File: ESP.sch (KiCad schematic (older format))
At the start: 2 parts, among them U301 LSF0204x, U302 ESP8266

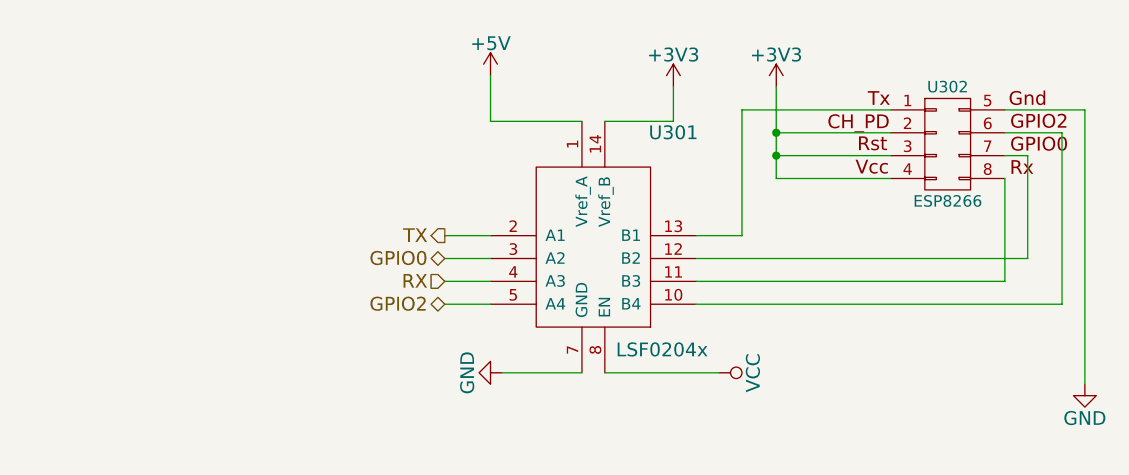
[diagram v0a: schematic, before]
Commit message: Redesign the board and add USB
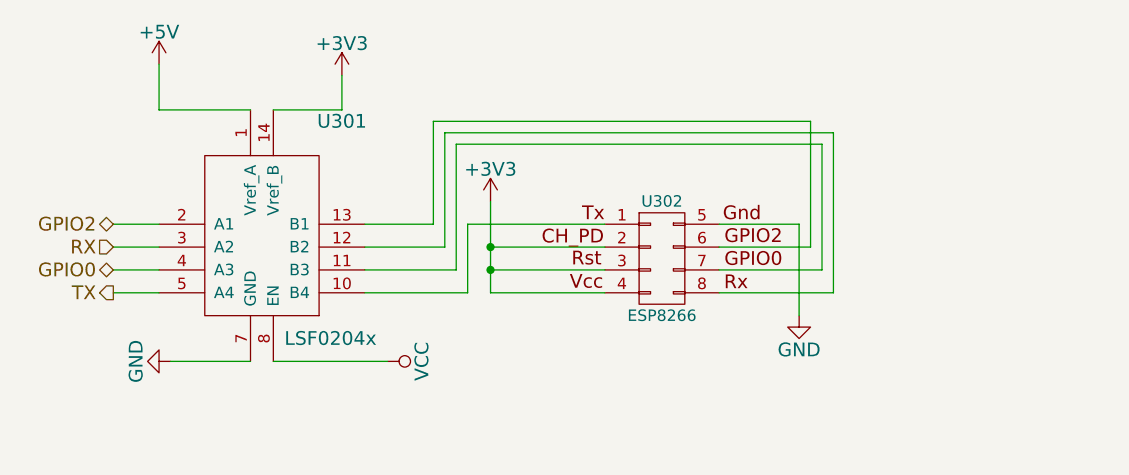
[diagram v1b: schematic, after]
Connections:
- net GPIO0: now also U301.4 (A3); no longer U301.3 (A2)
- net GPIO2: now also U301.2 (A1); no longer U301.5 (A4)
- net RX: now also U301.3 (A2); no longer U301.4 (A3)
- net TX: now also U301.5 (A4); no longer U301.2 (A1)
- net at U301.10 (B4): now also U302.1 (TX); no longer U302.6 (P4)
- net at U301.11 (B3): now also U302.7 (P6); no longer U302.8 (P8)
- net at U301.12 (B2): now also U302.8 (P8); no longer U302.7 (P6)
- net at U301.13 (B1): now also U302.6 (P4); no longer U302.1 (TX)
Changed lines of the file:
@@
 $Comp
 L LSF0204x U301
-U 1 1 55337A29
-P 4550 2300
-F 0 "U301" H 4900 2800 60  0000 C CNN
-F 1 "LSF0204x" H 4850 1850 60  0000 C CNN
-F 2 "" H 4550 2300 60  0000 C CNN
-F 3 "" H 4550 2300 60  0000 C CNN
-	1    4550 2300
+U 1 1 5538DE80
+P 3100 2250
+F 0 "U301" H 3450 2750 60  0000 C CNN
+F 1 "LSF0204x" H 3400 1800 60  0000 C CNN
+F 2 "" H 3100 2250 60  0000 C CNN
+F 3 "" H 3100 2250 60  0000 C CNN
+	1    3100 2250
 	1    0    0    -1
 $EndComp
 $Comp
 L ESP8266 U302
-U 1 1 55337A30
-P 6100 1850
-F 0 "U302" H 6100 2100 50  0000 C CNN
-F 1 "ESP8266" H 6100 1600 50  0000 C CNN
-F 2 "" H 6100 650 60  0000 C CNN
-F 3 "" H 6100 650 60  0000 C CNN
-	1    6100 1850
+U 1 1 5538DE86
+P 4850 2350
+F 0 "U302" H 4850 2600 50  0000 C CNN
+F 1 "ESP8266" H 4850 2100 50  0000 C CNN
+F 2 "" H 4850 1150 60  0000 C CNN
+F 3 "" H 4850 1150 60  0000 C CNN
+	1    4850 2350
+	1    0    0    -1
+$EndComp
+$Comp
+L VCC #PWR012
+U 1 1 5538DE95
+P 3650 2800
+F 0 "#PWR012" H 3650 2650 60  0001 C CNN
+F 1 "VCC" H 3650 2950 60  0000 C CNN
+F 2 "" H 3650 2800 60  0000 C CNN
+F 3 "" H 3650 2800 60  0000 C CNN
+	1    3650 2800
+	0    1    1    0
+$EndComp
+$Comp
+L +5V #PWR013
+U 1 1 5538DE9F
+P 2650 1500
+F 0 "#PWR013" H 2650 1350 60  0001 C CNN
+F 1 "+5V" H 2650 1640 60  0000 C CNN
+F 2 "" H 2650 1500 60  0000 C CNN
+F 3 "" H 2650 1500 60  0000 C CNN
+	1    2650 1500
+	1    0    0    -1
+$EndComp
+$Comp
+L +3V3 #PWR014
+U 1 1 5538DEAA
+P 3450 1550
+F 0 "#PWR014" H 3450 1400 60  0001 C CNN
+F 1 "+3V3" H 3450 1690 60  0000 C CNN
+F 2 "" H 3450 1550 60  0000 C CNN
+F 3 "" H 3450 1550 60  0000 C CNN
+	1    3450 1550
+	1    0    0    -1
+$EndComp
+$Comp
+L GND #PWR015
+U 1 1 5538DEB0
+P 2700 2800
+F 0 "#PWR015" H 2700 2550 60  0001 C CNN
+F 1 "GND" H 2700 2650 60  0000 C CNN
+F 2 "" H 2700 2800 60  0000 C CNN
+F 3 "" H 2700 2800 60  0000 C CNN
+	1    2700 2800
+	0    1    1    0
+$EndComp
+$Comp
+L GND #PWR016
+U 1 1 5538DEB7
+P 5450 2600
+F 0 "#PWR016" H 5450 2350 60  0001 C CNN
+F 1 "GND" H 5450 2450 60  0000 C CNN
+F 2 "" H 5450 2600 60  0000 C CNN
+F 3 "" H 5450 2600 60  0000 C CNN
+	1    5450 2600
+	1    0    0    -1
+$EndComp
+Text HLabel 2450 2500 0    60   Output ~ 0
+TX
+Text HLabel 2450 2400 0    60   BiDi ~ 0
+GPIO0
+Text HLabel 2450 2300 0    60   Input ~ 0
+RX
+Text HLabel 2450 2200 0    60   BiDi ~ 0
+GPIO2
+$Comp
+L +3V3 #PWR017
+U 1 1 5538DEC8
+P 4100 2100
+F 0 "#PWR017" H 4100 1950 60  0001 C CNN
+F 1 "+3V3" H 4100 2240 60  0000 C CNN
+F 2 "" H 4100 2100 60  0000 C CNN
+F 3 "" H 4100 2100 60  0000 C CNN
+	1    4100 2100
 	1    0    0    -1
 $EndComp
 Wire Wire Line
-	6350 2000 6350 2450
+	3150 2800 3650 2800
 Wire Wire Line
-	5000 2350 6450 2350
+	2650 1700 3050 1700
 Wire Wire Line
-	6450 2350 6450 1900
+	2650 1500 2650 1700
 Wire Wire Line
-	6450 1900 6350 1900
+	3150 1700 3450 1700
 Wire Wire Line
-	5850 1700 5200 1700
+	3450 1700 3450 1550
 Wire Wire Line
-	5000 2550 6600 2550
+	4100 2500 4600 2500
 Wire Wire Line
-	6600 2550 6600 1800
+	4100 2400 4600 2400
 Wire Wire Line
-	6600 1800 6350 1800
+	4100 2300 4600 2300
 Wire Wire Line
-	4600 2850 5100 2850
-$Comp
-L VCC #PWR010
-U 1 1 55337A40
-P 5100 2850
-F 0 "#PWR010" H 5100 2700 60  0001 C CNN
-F 1 "VCC" H 5100 3000 60  0000 C CNN
-F 2 "" H 5100 2850 60  0000 C CNN
-F 3 "" H 5100 2850 60  0000 C CNN
-	1    5100 2850
-	0    1    1    0
-$EndComp
+	2700 2800 3050 2800
 Wire Wire Line
-	4100 1750 4500 1750
+	4100 2100 4100 2500
+Connection ~ 4100 2400
+Connection ~ 4100 2300
 Wire Wire Line
-	4100 1550 4100 1750
+	2650 2200 2450 2200
 Wire Wire Line
-	4600 1750 4900 1750
+	2450 2300 2650 2300
 Wire Wire Line
-	4900 1750 4900 1600
-$Comp
-L +5V #PWR011
-U 1 1 55337A4A
-P 4100 1550
-F 0 "#PWR011" H 4100 1400 60  0001 C CNN
-F 1 "+5V" H 4100 1690 60  0000 C CNN
-F 2 "" H 4100 1550 60  0000 C CNN
-F 3 "" H 4100 1550 60  0000 C CNN
-	1    4100 1550
-	1    0    0    -1
-$EndComp
+	2450 2400 2650 2400
 Wire Wire Line
-	6350 1700 6700 1700
+	2450 2500 2650 2500
 Wire Wire Line
-	6700 1700 6700 2900
+	4600 2200 4000 2200
 Wire Wire Line
-	5350 2000 5850 2000
+	4000 2200 4000 2500
 Wire Wire Line
-	5350 1900 5850 1900
+	4000 2500 3550 2500
 Wire Wire Line
-	5350 1800 5850 1800
-$Comp
-L +3V3 #PWR012
-U 1 1 55337A58
-P 4900 1600
-F 0 "#PWR012" H 4900 1450 60  0001 C CNN
-F 1 "+3V3" H 4900 1740 60  0000 C CNN
-F 2 "" H 4900 1600 60  0000 C CNN
-F 3 "" H 4900 1600 60  0000 C CNN
-	1    4900 1600
-	1    0    0    -1
-$EndComp
-$Comp
-L GND #PWR013
-U 1 1 55337A5E
-P 4150 2850
-F 0 "#PWR013" H 4150 2600 60  0001 C CNN
-F 1 "GND" H 4150 2700 60  0000 C CNN
-F 2 "" H 4150 2850 60  0000 C CNN
-F 3 "" H 4150 2850 60  0000 C CNN
-	1    4150 2850
-	0    1    1    0
-$EndComp
+	3550 2400 3950 2400
 Wire Wire Line
-	4150 2850 4500 2850
-$Comp
-L GND #PWR014
-U 1 1 55337A65
-P 6700 2900
-F 0 "#PWR014" H 6700 2650 60  0001 C CNN
-F 1 "GND" H 6700 2750 60  0000 C CNN
-F 2 "" H 6700 2900 60  0000 C CNN
-F 3 "" H 6700 2900 60  0000 C CNN
-	1    6700 2900
-	1    0    0    -1
-$EndComp
+	3950 2400 3950 1850
 Wire Wire Line
-	4100 2250 3900 2250
+	3950 1850 5550 1850
 Wire Wire Line
-	4100 2450 3900 2450
+	5550 1850 5550 2400
 Wire Wire Line
-	4100 2550 3900 2550
+	5550 2400 5100 2400
 Wire Wire Line
-	5000 2250 5200 2250
+	3550 2300 3900 2300
 Wire Wire Line
-	5200 2250 5200 1700
+	3900 2300 3900 1800
 Wire Wire Line
-	6350 2450 5000 2450
-Text HLabel 3900 2250 0    60   Output ~ 0
-TX
-Text HLabel 3900 2350 0    60   BiDi ~ 0
-GPIO0
-Text HLabel 3900 2450 0    60   Input ~ 0
-RX
-Text HLabel 3900 2550 0    60   BiDi ~ 0
-GPIO2
+	3900 1800 5600 1800
 Wire Wire Line
-	4100 2350 3900 2350
-$Comp
-L +3V3 #PWR015
-U 1 1 5535FAE0
-P 5350 1600
-F 0 "#PWR015" H 5350 1450 60  0001 C CNN
-F 1 "+3V3" H 5350 1740 60  0000 C CNN
-F 2 "" H 5350 1600 60  0000 C CNN
-F 3 "" H 5350 1600 60  0000 C CNN
-	1    5350 1600
-	1    0    0    -1
-$EndComp
+	5600 1800 5600 2500
 Wire Wire Line
-	5350 1600 5350 2000
-Connection ~ 5350 1900
-Connection ~ 5350 1800
+	5600 2500 5100 2500
+Wire Wire Line
+	3550 2200 3850 2200
+Wire Wire Line
+	3850 2200 3850 1750
+Wire Wire Line
+	3850 1750 5500 1750
+Wire Wire Line
+	5500 1750 5500 2300
+Wire Wire Line
+	5500 2300 5100 2300
+Wire Wire Line
+	5100 2200 5450 2200
+Wire Wire Line
+	5450 2200 5450 2600
 $EndSCHEMATC

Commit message: Version 0.2
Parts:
- U301: footprint (none) -> ab2_tssop:AB2_TSSOP14
- U302: footprint (none) -> footprints:ESP8266_2
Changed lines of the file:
@@
 EESchema Schematic File Version 2
+LIBS:espduino-rescue
 LIBS:power
 LIBS:device
@@
 LIBS:memory
 LIBS:xilinx
-LIBS:special
 LIBS:microcontrollers
 LIBS:dsp
@@
 LIBS:valves
 LIBS:littlebush
+LIBS:ab2_7segment
+LIBS:ab2_audio
+LIBS:ab2_buffer
+LIBS:ab2_capacitor
+LIBS:ab2_connectivity
+LIBS:ab2_dac
+LIBS:ab2_diode
+LIBS:ab2_gpio_expansion
+LIBS:ab2_header
+LIBS:ab2_idc
+LIBS:ab2_inductor
+LIBS:ab2_input_devices
+LIBS:ab2_jumper
+LIBS:ab2_lcd
+LIBS:ab2_led
+LIBS:ab2_opamp
+LIBS:ab2_pot
+LIBS:ab2_power
+LIBS:ab2_regulator
+LIBS:ab2_relay
+LIBS:ab2_resistor
+LIBS:ab2_sensor
+LIBS:ab2_stepper
+LIBS:ab2_supply
+LIBS:ab2_terminal_block
+LIBS:ab2_test
+LIBS:ab2_transistor
+LIBS:ab2_uC
+LIBS:ab2_usb
+LIBS:ab2_xtal
 LIBS:espduino-cache
 EELAYER 25 0
@@
 $Descr A4 11693 8268
 encoding utf-8
-Sheet 3 5
+Sheet 3 6
 Title ""
 Date ""
@@
 F 0 "U301" H 3450 2750 60  0000 C CNN
 F 1 "LSF0204x" H 3400 1800 60  0000 C CNN
-F 2 "" H 3100 2250 60  0000 C CNN
+F 2 "ab2_tssop:AB2_TSSOP14" H 3100 2250 60  0001 C CNN
 F 3 "" H 3100 2250 60  0000 C CNN
 	1    3100 2250
@@
 F 0 "U302" H 4850 2600 50  0000 C CNN
 F 1 "ESP8266" H 4850 2100 50  0000 C CNN
-F 2 "" H 4850 1150 60  0000 C CNN
+F 2 "footprints:ESP8266_2" H 4850 1150 60  0001 C CNN
 F 3 "" H 4850 1150 60  0000 C CNN
 	1    4850 2350

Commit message: Minor changes
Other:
- note added: "This is wrong, VRefA must be the lower voltage\n"
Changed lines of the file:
@@
 Wire Wire Line
 	5450 2200 5450 2600
+Text Notes 2800 3200 0    60   ~ 0
+This is wrong, VRefA must be the lower voltage\n
 $EndSCHEMATC
